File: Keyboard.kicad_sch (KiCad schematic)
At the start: 80 parts, among them J1 USB_C_Receptacle, J2 Conn_02x01_Row_Letter_First, K1 KEYSW, K10 KEYSW, K11 KEYSW, K12 KEYSW, K13 KEYSW, K14 KEYSW, K15 KEYSW, K16 KEYSW, K17 KEYSW, K18 KEYSW, K19 KEYSW, K2 KEYSW, K20 KEYSW, K21 KEYSW, K22 KEYSW, K23 KEYSW, K24 KEYSW, K25 KEYSW, K26 KEYSW, K27 KEYSW, K28 KEYSW, K29 KEYSW, K3 KEYSW, K30 KEYSW, K4 KEYSW, K5 KEYSW, K6 KEYSW, K7 KEYSW, K8 KEYSW, K9 KEYSW, U1 ESP32-C3FH4, U3 MCP73831-2-OT, U4 LM1117DT-3.3

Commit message: keyboard progress
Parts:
- removed C4: 10uF, symbol Device:C
- removed C5: 100uF, symbol Device:C
- removed D10, D11, D12, D13, D14, D15, D16, D17, D18, D19, D2, D20, D21, D22, D23, D24, D25, D26, D28, D29, D3, D30, D31, D32, D4, D5, D6, D7, D8, D9: D, symbol Device:D
- removed K1, K10, K11, K12, K13, K14, K15, K16, K17, K18, K19, K2, K20, K21, K22, K23, K24, K25, K26, K27, K28, K29, K3, K30, K4, K5, K6, K7, K8, K9: KEYSW, symbol keyboard_parts2:KEYSW
- removed R5, R6: 500, symbol Device:R
- added C1, C6: 1uF, symbol Device:C
- added C7, C8: 10uF, symbol Device:C
- added J3: FFC2B35-16-G_REVA2, FFC2B35-16-G_REVA2:GCT_FFC2B35-16-G_REVA2, symbol FFC2B35-16-G_REVA2:FFC2B35-16-G_REVA2
- added R11: 680kOhm, symbol Device:R
- added R12: 5.1kOhm, symbol Device:R
- added U2: CY8C6347BZI-BLD33, CY8C6347BZI-BLD33:BGA116N50P10X12_520X640X70N, symbol CY8C6347BZI-BLD33:CY8C6347BZI-BLD33
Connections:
- net +5V: now also J1.A1 (GND), J1.A12 (GND), J1.B1 (GND), J1.B12 (GND), U4.1 (GND), C7.2, C8.2, J3.16, J3.6, R11.2, R12.1
- net MOSI: now also J3.12
- net OLED_CS: now also J3.8
- net OLED_DC: now also J3.10
- net SCK: now also J3.11
- net VBAT: now also BT2.1 (+), C3.1, J2.a1 (Pin_a1), U3.3 (V_{BAT}), J3.5, J3.7
- net Vin: now also U1.7 (CHIP_EN)
- new net: C7.1, J3.14
- new net: C1.1, J3.1
- new net: J3.13, R11.1
- new net: C8.1, J3.15
- new net: C1.2, J3.2
- new net: C6.1, J3.3
- new net: C6.2, J3.4
- new net: U2.B2 (VSS), U2.B9 (VSS), U2.D1 (VSS), U2.H2 (VSS), U2.H9 (VSS)
- new net: U2.J1 (VSSR), U2.K2 (VSSR), U2.K3 (VSSR), U2.K4 (VSSR), U2.K5 (VSSR), U2.L1 (VSSR), U2.L3 (VSSR), U2.L4 (VSSR), U2.L5 (VSSR), U2.M3 (VSSR), U2.M8 (VSSR)
- new net OLED_RST: J3.9, R12.2
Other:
- removed sheet LCD schematic
- added sheet Switch_Grid (Switch_Grid.kicad_sch)
- note removed: "Keyboard Matrix"
- moved on the sheet: BT2, C, C2, C3, D1, J1, J2, R1, R2, R3, R4, R7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

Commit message: started working with another microcontroller
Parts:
- removed U2: CY8C6347BZI-BLD33, CY8C6347BZI-BLD33:BGA116N50P10X12_520X640X70N, symbol CY8C6347BZI-BLD33:CY8C6347BZI-BLD33
- added C: 1uF, symbol Device:C
- added C_Ceramic: .1uF, symbol Device:C
- added C_Electrolytic: 22uF, symbol Device:C
- added R10, R9: 10k ohm, symbol Device:R
- added U5: ESP32-S3-WROOM-1-N16R2, ESP32-S3-WROOM-1-N16R2:XCVR_ESP32-S3-WROOM-1-N16R2, symbol ESP32-S3-WROOM-1-N16R2:ESP32-S3-WROOM-1-N16R2
- renumbered C8 to C10, C7 to C4, C1 to C5, C6 to C9, J3 to J4, R11 to R5, R12 to R6
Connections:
- net +5V: now also C_Ceramic.2, C_Electrolytic.2, R10.1, R9.1, U5.1 (GND), U5.40 (GND), U5.41_1 (GND), U5.41_2 (GND), U5.41_3 (GND), U5.41_4 (GND), U5.41_5 (GND), U5.41_6 (GND), U5.41_7 (GND), U5.41_8 (GND), U5.41_9 (GND)
- net D+: now also U5.14 (IO20)
- net D-: now also U5.13 (IO19)
- net Vin renamed EN In
- net EN In: now also C.1, C_Ceramic.1, C_Electrolytic.1, U5.2 (3V3)
- new net: R10.2, U5.27 (IO0)
- new net: C.2, R9.2, U5.3 (EN)
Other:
- moved on the sheet: U1

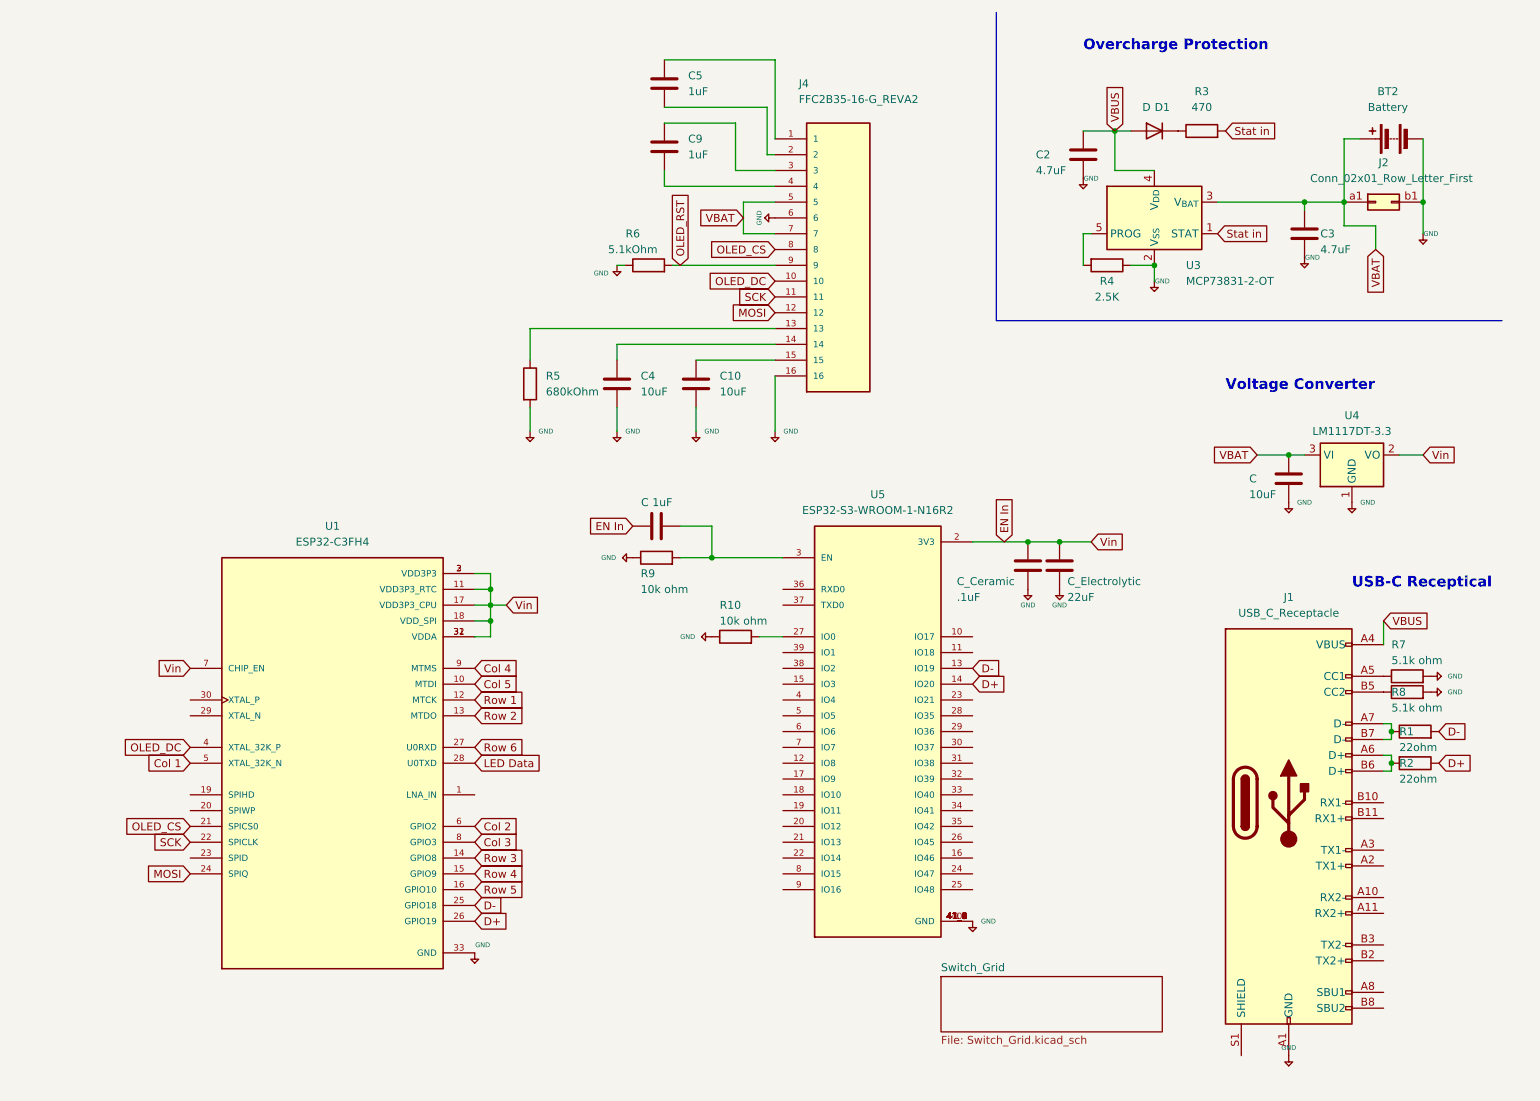
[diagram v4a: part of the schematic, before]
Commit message: added mosfets for clearly marking what is powering board
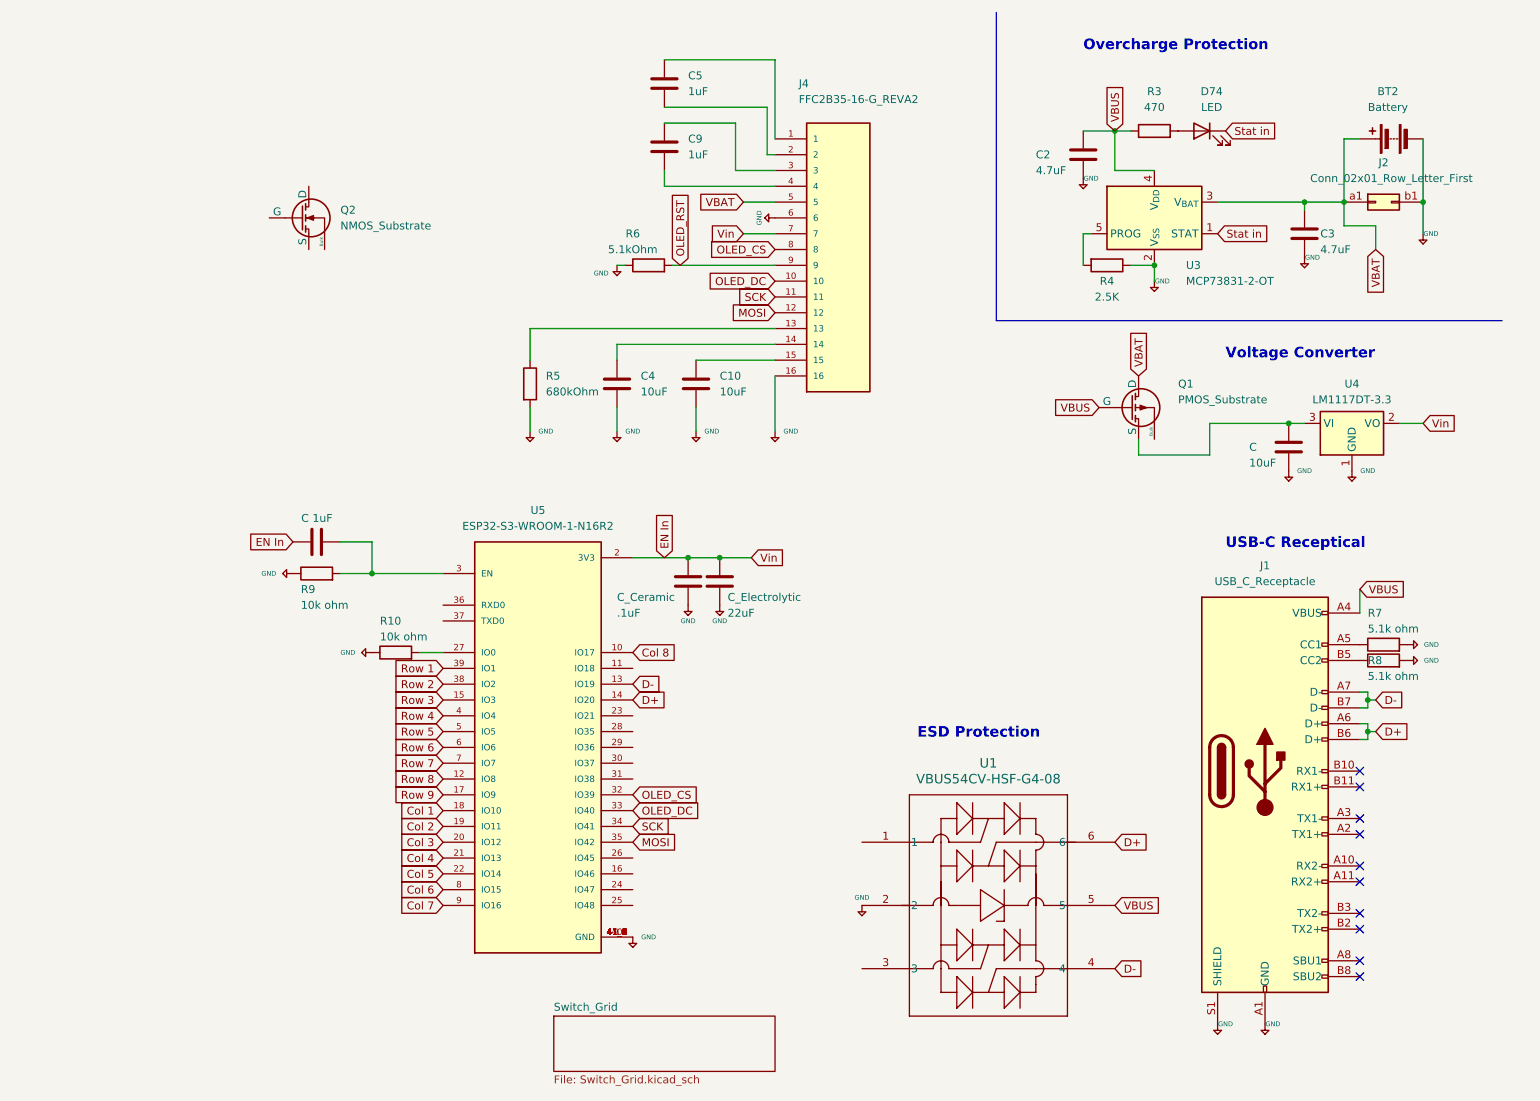
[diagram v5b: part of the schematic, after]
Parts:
- removed D1: D, symbol Device:D
- removed R1, R2: 22ohm, symbol Device:R
- removed U1: ESP32-C3FH4, ESP32-C3FH4:QFN50P500X500X90-33N, symbol keyboard_parts:ESP32-C3FH4
- added D74: LED, symbol Device:LED
- added Q1: PMOS_Substrate, symbol Simulation_SPICE:PMOS_Substrate
- added Q2: NMOS_Substrate, symbol Simulation_SPICE:NMOS_Substrate
- added U1: VBUS54CV-HSF-G4-08, SMT_CV-HSF-G4-08_VIS, symbol VBUS54CV-HSF-G4-08:VBUS54CV-HSF-G4-08
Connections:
- net +5V: now also J1.S1 (SHIELD), U1.2
- net Col 1: now also U5.18 (IO10)
- net Col 2: now also U5.19 (IO11)
- net Col 3: now also U5.20 (IO12)
- net Col 4: now also U5.21 (IO13)
- net Col 5: now also U5.22 (IO14)
- net D+: now also J1.A6 (D+), J1.B6 (D+), U1.6
- net D-: now also J1.A7 (D-), J1.B7 (D-), U1.4
- net EN In: now also J4.7
- net MOSI: now also U5.35 (IO42)
- net OLED_CS: now also U5.32 (IO39)
- net OLED_DC: now also U5.33 (IO40)
- net Row 1: now also U5.39 (IO1)
- net Row 2: now also U5.38 (IO2)
- net Row 3: now also U5.15 (IO3)
- net Row 4: now also U5.4 (IO4)
- net Row 5: now also U5.5 (IO5)
- net Row 6: now also U5.6 (IO6)
- net SCK: now also U5.34 (IO41)
- net Stat in: now also D74.1 (K); no longer R3.2
- net VBAT: now also Q1.1 (D); no longer C.1, J4.7, U4.3 (VI)
- net VBUS: now also R3.1, Q1.2 (G), U1.5
- net Col 8: now reaches U5.10 (IO17)
- net Row 8: now reaches U5.12 (IO8)
- net Row 9: now reaches U5.17 (IO9)
- net Row 7: now reaches U5.7 (IO7)
- net Col 6: now reaches U5.8 (IO15)
- net Col 7: now reaches U5.9 (IO16)
- new net: D74.2 (A), R3.2
- new net: C.1, Q1.3 (S), U4.3 (VI)
- no-connect marks 0 -> 10
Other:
- note added: "ESD Protection"
- moved on the sheet: C, C_Ceramic, C_Electrolytic, J1, R10, R3, R7, R8, R9, U4, U5

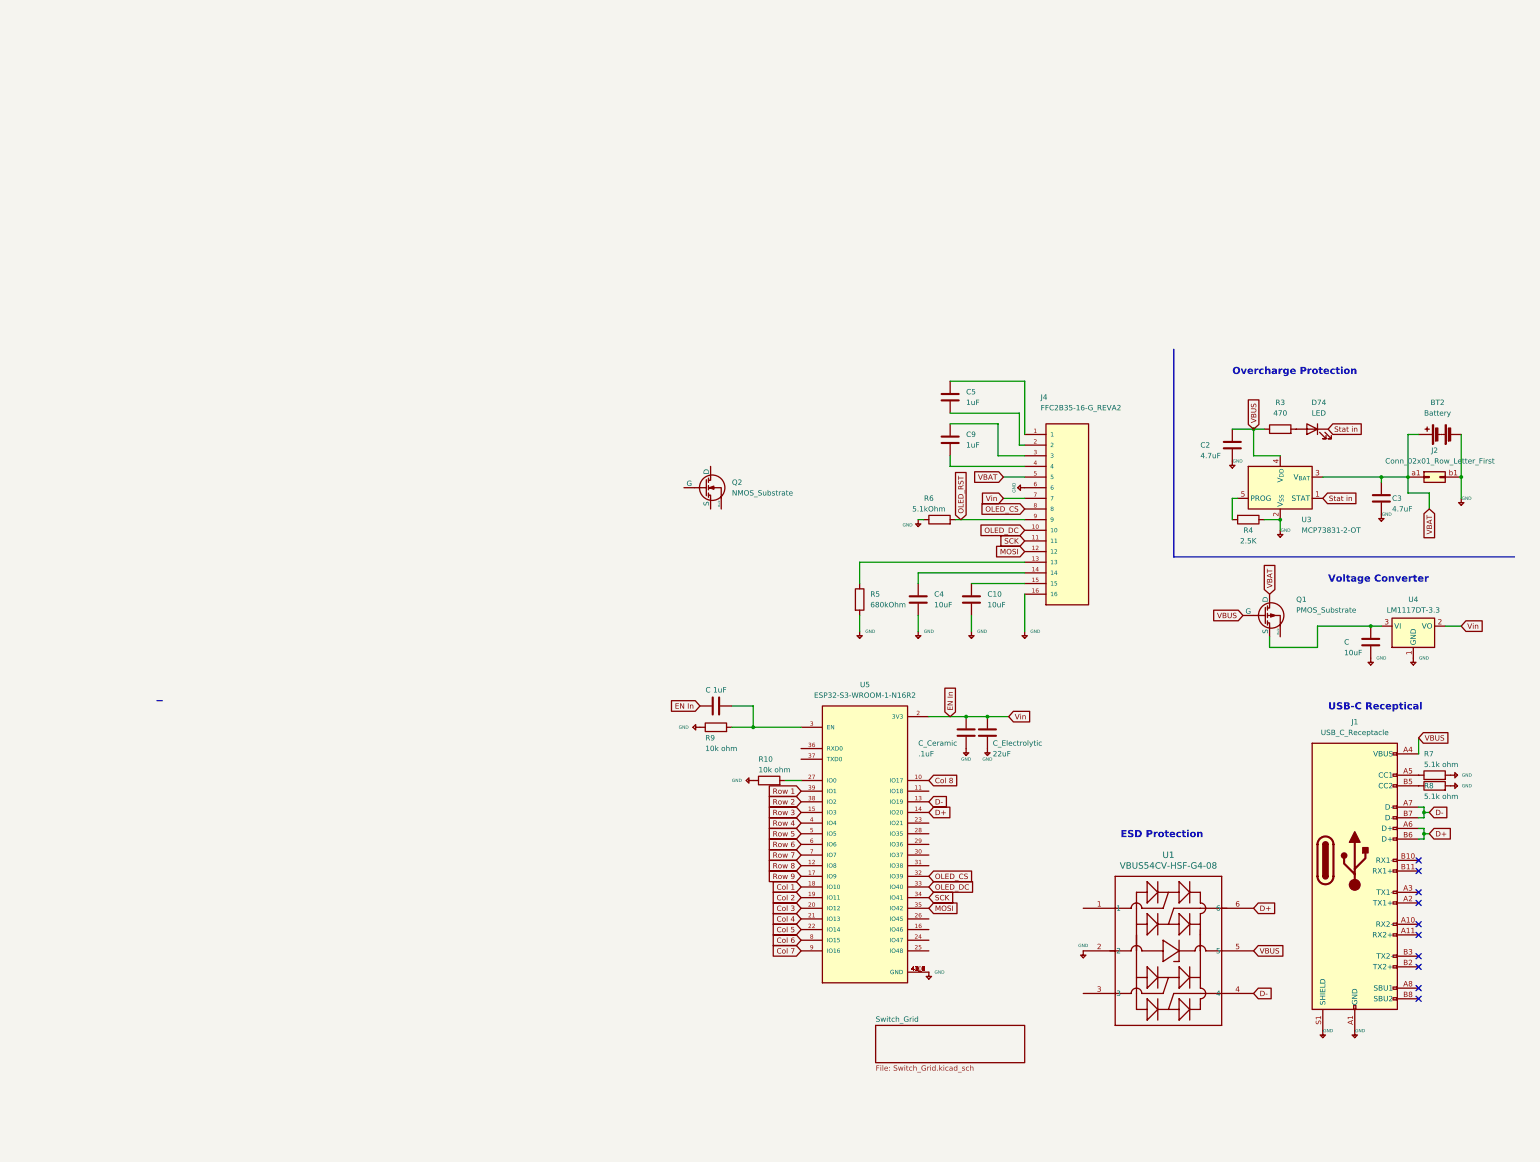
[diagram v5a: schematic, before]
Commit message: started on pcb
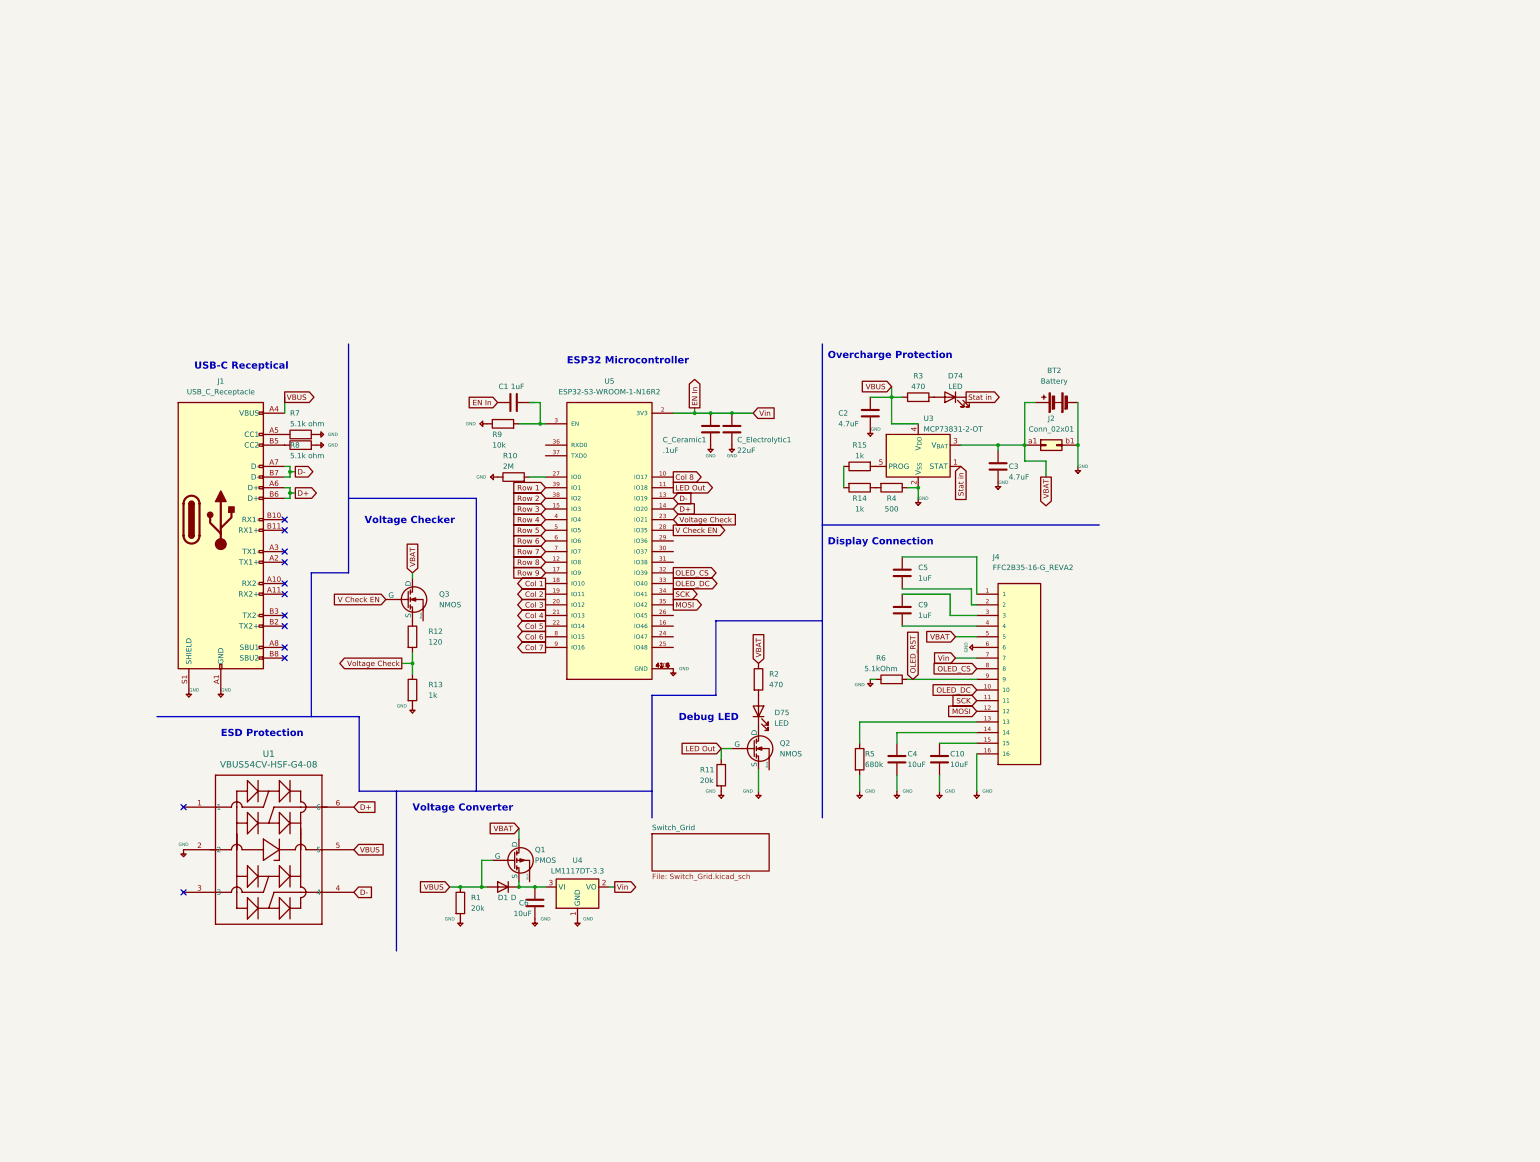
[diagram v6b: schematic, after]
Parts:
- added D1: D, Diode_SMD:D_0603_1608Metric_Pad1.05x0.95mm_HandSolder, symbol Device:D
- added D75: LED, LED_SMD:LED_0603_1608Metric, symbol Device:LED
- added Q3: NMOS, keyboard_parts:MOS_FET_SOT23-3_HSOL, symbol Simulation_SPICE:NMOS_Substrate
- added R1, R11: 20k, Resistor_SMD:R_0402_1005Metric, symbol Device:R
- added R12: 120, Resistor_SMD:R_0402_1005Metric, symbol Device:R
- added R13, R14, R15: 1k, Resistor_SMD:R_0402_1005Metric, symbol Device:R
- added R2: 470, Resistor_SMD:R_0402_1005Metric, symbol Device:R
- C1, C6: renamed from C; footprint (none) -> Capacitor_SMD:C_0402_1005Metric
- C10, C2, C3, C4, C5, C9: footprint (none) -> Capacitor_SMD:C_0402_1005Metric
- C_Ceramic1: renamed from C_Ceramic; footprint (none) -> Capacitor_SMD:C_0402_1005Metric
- C_Electrolytic1: renamed from C_Electrolytic; footprint (none) -> Capacitor_SMD:C_0805_2012Metric
- D74: footprint (none) -> LED_SMD:LED_0603_1608Metric
- J1: footprint (none) -> Connector_USB:USB_C_Receptacle_Amphenol_12401548E4-2A
- J2: value Conn_02x01_Row_Letter_First -> Conn_02x01; footprint (none) -> Connector_Molex:Molex_KK-254_AE-6410-02A_1x02_P2.54mm_Vertical
- J4: footprint FFC2B35-16-G_REVA2:GCT_FFC2B35-16-G_REVA2 -> keyboard_parts:GCT_FFC2B35-16-G_REVA2
- Q1: value PMOS_Substrate -> PMOS; footprint (none) -> keyboard_parts:MOS_FET_SOT23-3_HSOL
- Q2: value NMOS_Substrate -> NMOS; footprint (none) -> keyboard_parts:MOS_FET_SOT23-3_HSOL
- R10: value 10k ohm -> 2M; footprint (none) -> Resistor_SMD:R_0402_1005Metric
- R3, R6, R7, R8: footprint (none) -> Resistor_SMD:R_0402_1005Metric
- R4: value 2.5K -> 500; footprint (none) -> Resistor_SMD:R_0603_1608Metric
- R5: value 680kOhm -> 680k; footprint (none) -> Resistor_SMD:R_0402_1005Metric
- R9: value 10k ohm -> 10k; footprint (none) -> Resistor_SMD:R_0402_1005Metric
- U1: footprint SMT_CV-HSF-G4-08_VIS -> keyboard_parts:SMT_CV-HSF-G4-08_VIS
- U5: footprint ESP32-S3-WROOM-1-N16R2:XCVR_ESP32-S3-WROOM-1-N16R2 -> keyboard_parts:XCVR_ESP32-S3-WROOM-1-N16R2
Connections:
- net +5V: now also Q2.3 (S), R1.2, R11.2, R13.2
- net VBAT: now also Q3.1 (D), R2.1
- net VBUS: now also D1.2 (A), R1.1
- net LED Out: now reaches U5.11 (IO18)
- net LED Out: now also Q2.2 (G), R11.1
- net Voltage Check: now reaches U5.23 (IO21)
- net Voltage Check: now also R12.2, R13.1
- net V Check EN: now reaches U5.28 (IO35)
- net V Check EN: now also Q3.2 (G)
- net at Q2.1 (D): now also D75.1 (K)
- net at U3.5 (PROG): now also R15.2; no longer R4.2
- net at C6.1, Q1.3 (S), U4.3 (VI): now also D1.1 (K)
- new net: Q3.3 (S), R12.1
- new net: D75.2 (A), R2.2
- new net: R14.2, R15.1
- new net: R14.1, R4.2
- no-connect marks 10 -> 12
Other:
- note added: "Debug LED"
- note added: "Display Connection"
- note added: "ESP32 Microcontroller"
- note added: "Voltage Checker"
- moved on the sheet: BT2, C1, C10, C2, C3, C4, C5, C6, C9, C_Ceramic1, C_Electrolytic1, D74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
